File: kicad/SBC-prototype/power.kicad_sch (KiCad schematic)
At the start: 1 part, among them J1 Barrel_Jack

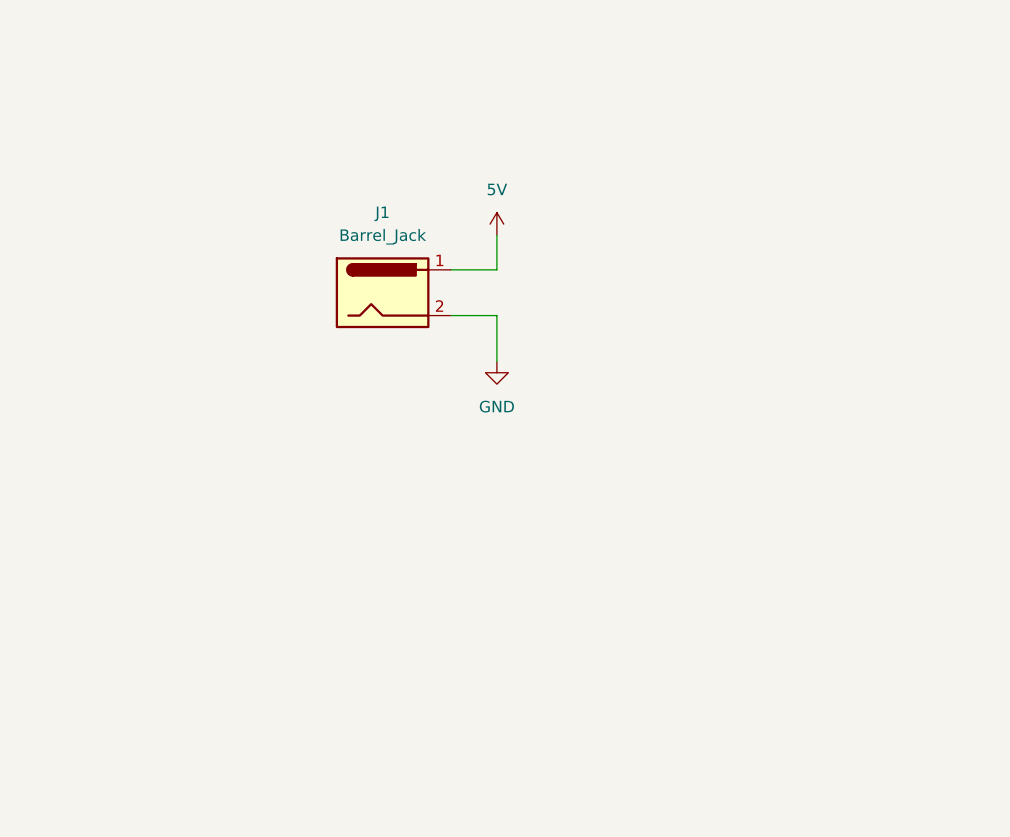
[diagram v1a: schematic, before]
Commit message: Added a power LED, decoupling caps for the power supply and each IC
- Power supply now has a 100uF polarized cap on the 5V rail and 0.1uF
  caps on each of the IC power pins.
- Going to add a VIA to drive an LCD display and then build it
- Haven't looked at footprints yet
- Power input needs a SPDT power switch (I like the power switch like
  what is on the Xilinx FPGA eval boards).
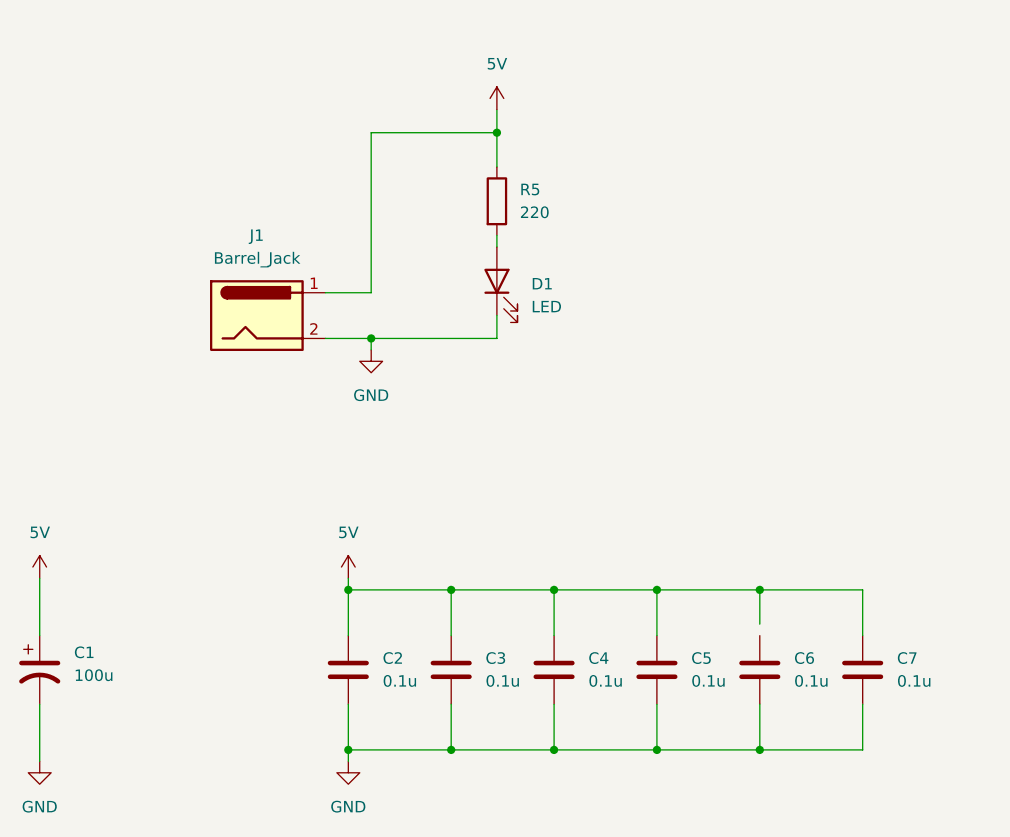
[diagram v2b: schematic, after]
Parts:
- added C1: 100u, symbol Device:C_Polarized_US
- added C2, C3, C4, C5, C6, C7: 0.1u, symbol Device:C
- added D1: LED, symbol Device:LED
- added R5: 220, symbol Device:R
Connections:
- net 5V: now also C1.1, C2.1, C3.1, C4.1, C5.1, C7.1, R5.1
- net GND: now also C1.2, C2.2, C3.2, C4.2, C5.2, C6.2, C7.2, D1.1 (K)
- new net: D1.2 (A), R5.2
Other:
- moved on the sheet: J1

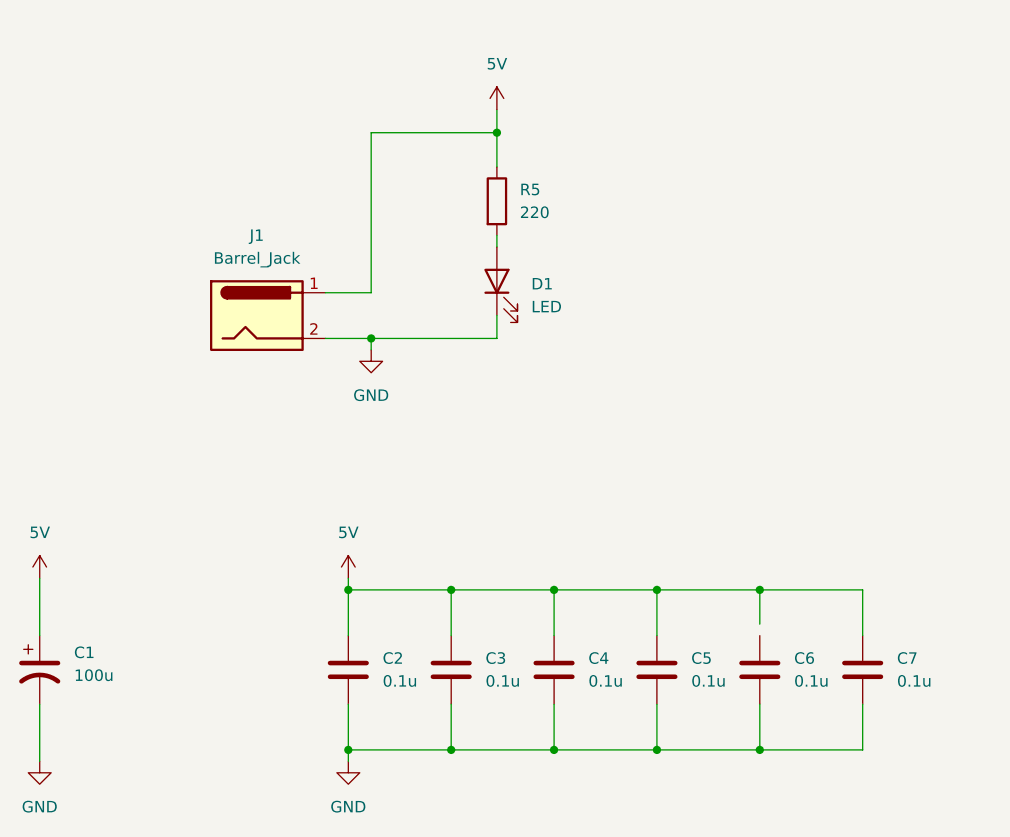
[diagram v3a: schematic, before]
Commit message: Fixed a ton of DRC errors and warnings
- VIA 1 is still unconnected since it's on the breadboard that way and I
  haven't hooked it to anything yet
- All the parts in the library have changed because I've modified my own
  versions of them. I'm not sure if I should add my changes to the
  library or find a way to tell the tool that it's OK that those are
  updated.
- The 74HC00 NAND gate was completely broken and would have been an
  interesting problem to sort out during routing and placement
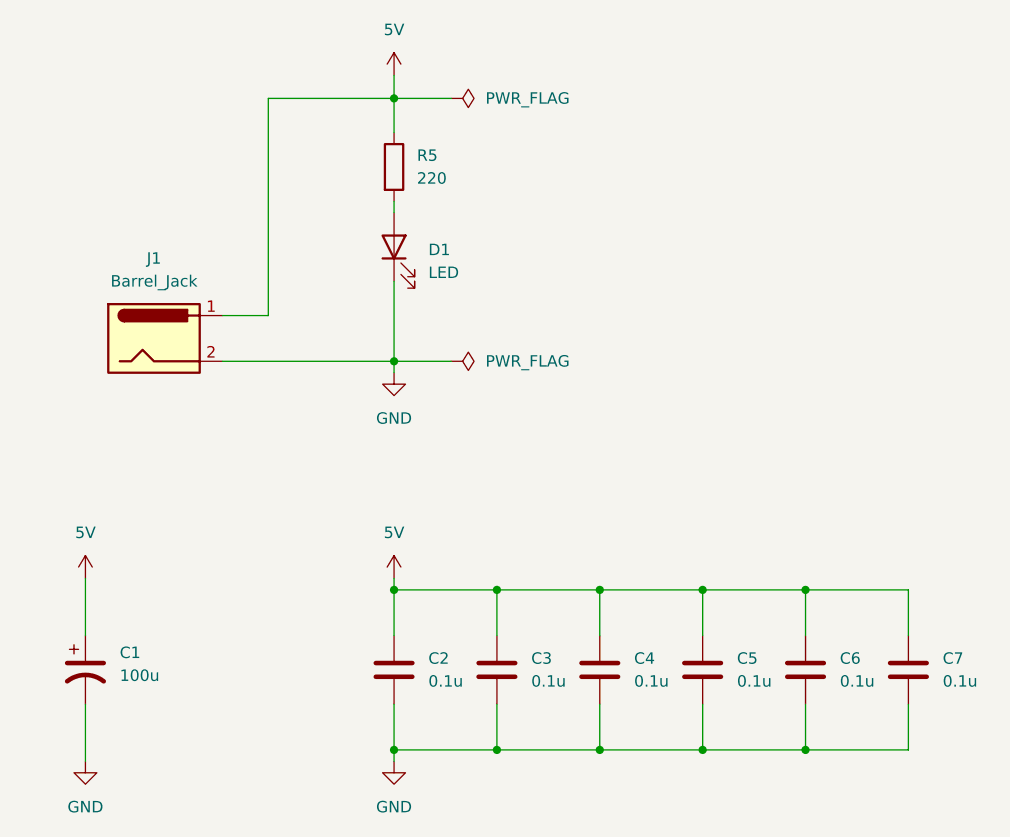
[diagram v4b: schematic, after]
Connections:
- net 5V: now also C6.1
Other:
- moved on the sheet: C1, C2, C3, C4, C5, C6, C7, D1, J1, R5
